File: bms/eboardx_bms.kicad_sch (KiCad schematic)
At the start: 28 parts, among them J1 Balance connector, P1 BAT+, P2 P+, P3 P-, P4 BAT-, Q1 MMBT3904, Q10 SE4060GB, Q11 SE4060GB, Q12 SE4060GB, Q13 SE4060GB, Q14 MMBT3904, Q2 SE4060GB, Q3 SE4060GB, Q4 SE4060GB, Q5 SE4060GB, Q6 SE4060GB, Q7 SE4060GB, Q8 SE4060GB, Q9 SE4060GB

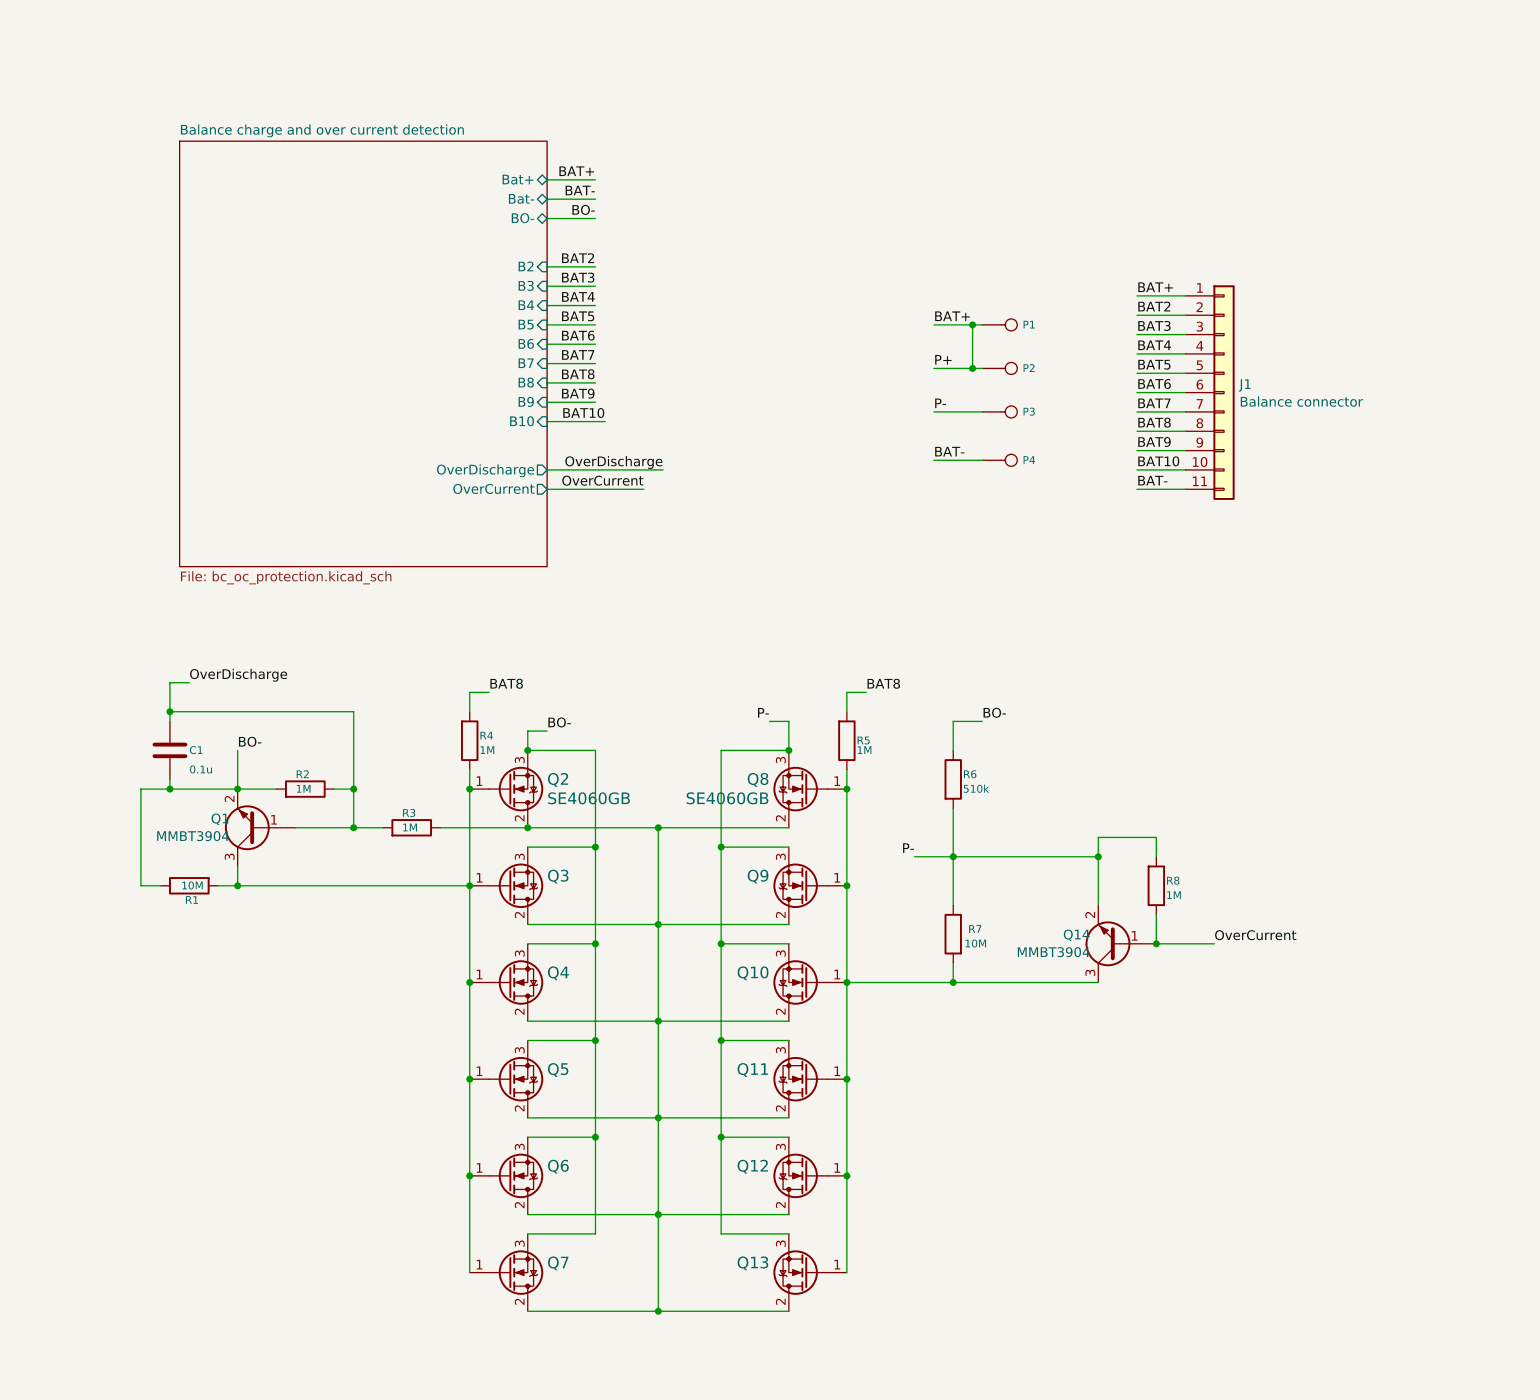
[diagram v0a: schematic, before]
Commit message: bms schematic
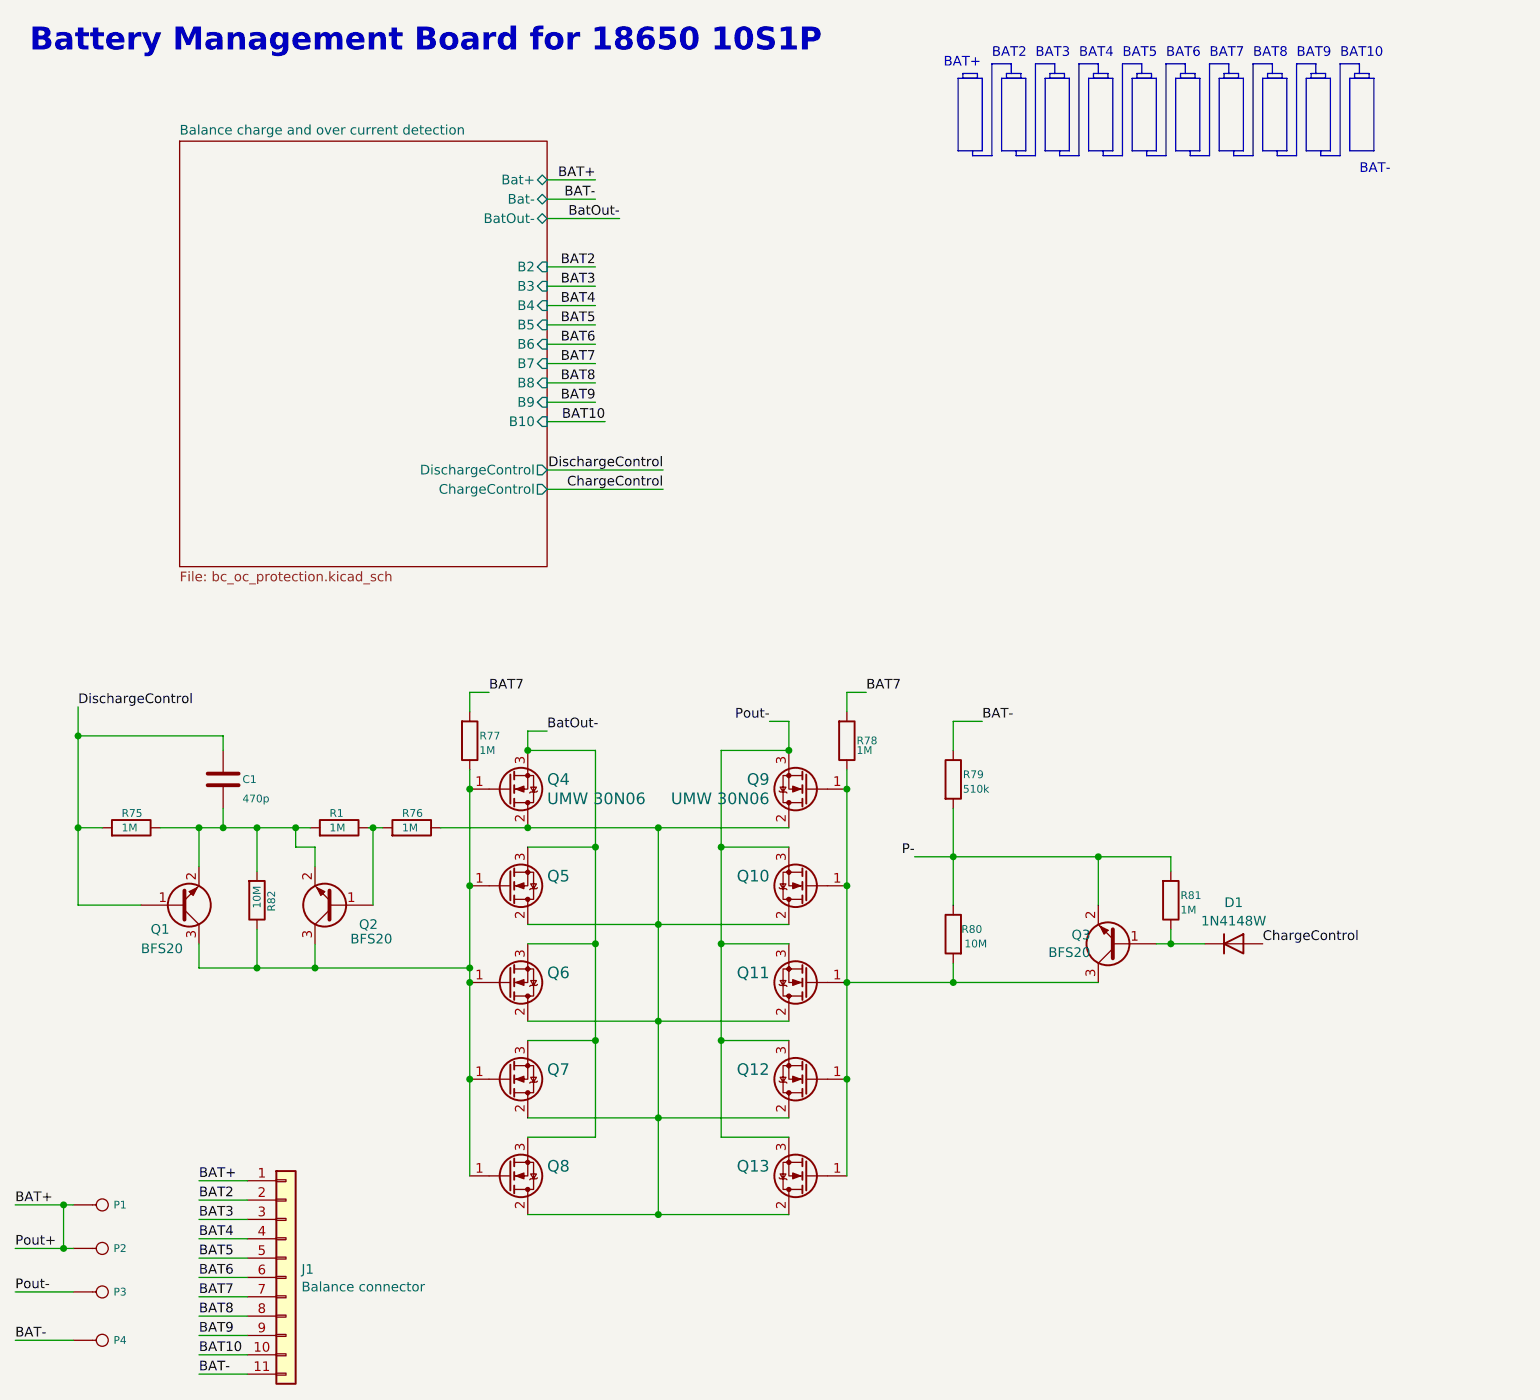
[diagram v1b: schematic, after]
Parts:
- removed Q13, Q7: SE4060GB, Package_TO_SOT_SMD:TO-252-2, symbol Device:Q_NMOS_GDS
- added D1: 1N4148W, Diode_SMD:D_SOD-123, symbol Device:D
- added Q1: BFS20, Package_TO_SOT_SMD:SOT-23, symbol Device:Q_NPN_BEC
- added R1: 1M, Resistor_SMD:R_0603_1608Metric, symbol Device:R
- C1: value 0.1u -> 470p
- Q10: renamed from Q9; value SE4060GB -> UMW 30N06
- Q11: renamed from Q10; value SE4060GB -> UMW 30N06
- Q12: renamed from Q11; value SE4060GB -> UMW 30N06
- Q13: renamed from Q12; value SE4060GB -> UMW 30N06
- Q2: renamed from Q1; value MMBT3904 -> BFS20
- Q3: renamed from Q14; value MMBT3904 -> BFS20
- Q4: renamed from Q2; value SE4060GB -> UMW 30N06
- Q5: renamed from Q3; value SE4060GB -> UMW 30N06
- Q6: renamed from Q4; value SE4060GB -> UMW 30N06
- Q7: renamed from Q5; value SE4060GB -> UMW 30N06
- Q8: renamed from Q6; value SE4060GB -> UMW 30N06
- Q9: renamed from Q8; value SE4060GB -> UMW 30N06
- renumbered R2 to R75, R3 to R76, R4 to R77, R5 to R78, R6 to R79, R7 to R80, R8 to R81, R1 to R82
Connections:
- net BAT-: now also R79.1
- net BAT7: now also R77.2, R78.2
- net BAT8: no longer R77.2, R78.2
- net P-: no longer P3.1, Q10.3 (S), Q11.3 (S), Q12.3 (S), Q13.3 (S), Q9.3 (S)
- net at Q2.3 (C), Q4.1 (G), Q5.1 (G)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: now also R82.1, Q1.3 (C); no longer R82.2
- net BO- renamed BatOut-
- net BatOut-: no longer C1.1, Q2.2 (E), R75.2, R79.1, R82.1
- net OverCurrent: no longer names the net of Q3.1 (B), R81.1
- net OverCurrent: now also D1.1 (K)
- net OverDischarge: no longer names the net of Q2.1 (B), R76.2
- net OverDischarge: now also R1.1; no longer C1.2, R75.1
- new net: C1.1, Q1.2 (E), Q2.2 (E), R1.2, R75.1, R82.2
- new net ChargeControl: D1.2 (A)
- new net DischargeControl: C1.2, Q1.1 (B), R75.2
- new net Pout-: P3.1, Q10.3 (S), Q11.3 (S), Q12.3 (S), Q13.3 (S), Q9.3 (S)
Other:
- sheet Balance charge and over current detection ports: added BatOut-, ChargeControl, DischargeControl; removed BO-, OverCurrent, OverDischarge
- note added: "BAT+"
- note added: "BAT-"
- note added: "BAT10"
- note added: "BAT2"
- note added: "BAT3"
- note added: "BAT4"
- note added: "BAT5"
- note added: "BAT6"
- note added: "BAT7"
- note added: "BAT8"
- note added: "BAT9"
- note added: "Battery Management Board for 18650 10S1P"
- moved on the sheet: C1, J1, P1, P2, P3, P4, Q2, R75, R81, R82

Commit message: bms change to 13s1p
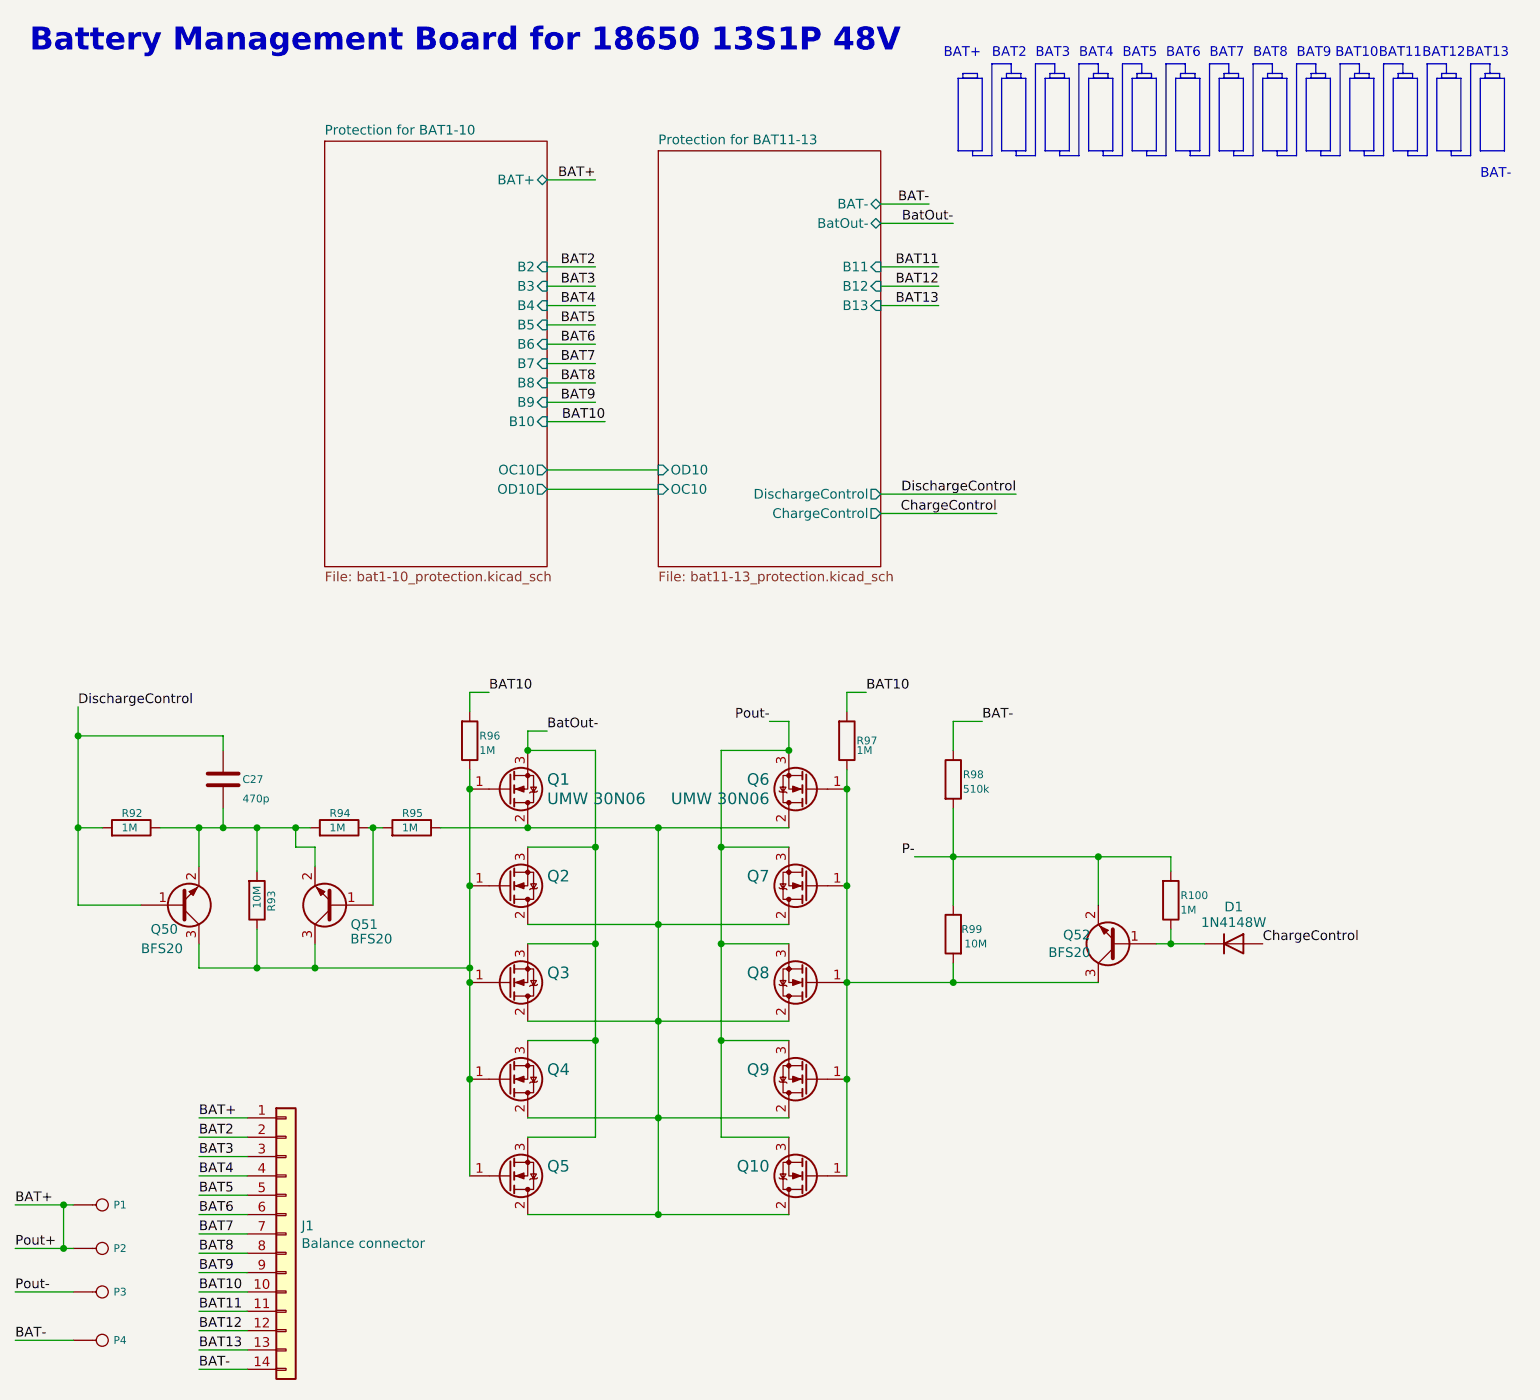
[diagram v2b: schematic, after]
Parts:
- J1: footprint Connector_JST:JST_PH_B11B-PH-K_1x11_P2.00mm_Vertical -> Connector_JST:JST_PH_B14B-PH-K_1x14_P2.00mm_Vertical; symbol Connector_Generic:Conn_01x11 -> Connector_Generic:Conn_01x14
- renumbered C1 to C27, Q4 to Q1, Q13 to Q10, Q5 to Q2, Q6 to Q3, Q7 to Q4, Q8 to Q5, Q1 to Q50, Q2 to Q51, Q3 to Q52, Q9 to Q6, Q10 to Q7, Q11 to Q8, Q12 to Q9, R81 to R100, R75 to R92, R82 to R93, R1 to R94, R76 to R95, R77 to R96, R78 to R97, R79 to R98, R80 to R99
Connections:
- net BAT-: now also J1.14 (Pin_14); no longer J1.11 (Pin_11)
- net BAT10: now also R96.2, R97.2
- net BAT7: no longer R96.2, R97.2
- new net BAT11: J1.11 (Pin_11)
- new net BAT12: J1.12 (Pin_12)
- new net BAT13: J1.13 (Pin_13)
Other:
- sheet Balance charge and over current detection renamed Protection for BAT1-10
- added sheet Protection for BAT11-13 (bat11-13_protection.kicad_sch)
- sheet Protection for BAT1-10: file bc_oc_protection.kicad_sch -> bat1-10_protection.kicad_sch
- sheet Protection for BAT1-10 ports: added BAT+, OC10, OD10; removed Bat+, Bat-, BatOut-, ChargeControl, DischargeControl
- note added: "BAT11"
- note added: "BAT12"
- note added: "BAT13"
- note added: "Battery Management Board for 18650 13S1P 48V"
- note removed: "Battery Management Board for 18650 10S1P"
